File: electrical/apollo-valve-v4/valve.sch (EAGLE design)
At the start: 40 parts, among them J1 VALVE2, J2 VALVE1, J7 455-1750-1-ND, U1 DRV8806-SSOP, U2 DRV8806-SSOP, U3 TPS54202

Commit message: Add initial layout for the Valve board. Fully routed, with plenty of room to potentially add the steppers back
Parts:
- added C9: 100uF, SparkFun-Capacitors:100UF-POLAR-25V-20%(ELEC)
- added J3: (no value), SparkFun-Connectors:CONN_023.5MM
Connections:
- net +24V: now also C9.+, J3.1
- net GND: now also C9.-, J3.2
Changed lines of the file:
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@@
 <part name="J7" library="SparkFun-Connectors" deviceset="CONN_03" device="" value="455-1750-1-ND"/>
 <part name="R6" library="apollo-ctrl-v4" deviceset="RESISTOR" device="0805-RES" value="100K"/>
+<part name="J3" library="SparkFun-Connectors" deviceset="CONN_02" device="3.5MM"/>
+<part name="GND10" library="supply1" deviceset="GND" device=""/>
+<part name="P+6" library="supply1" deviceset="+24V" device=""/>
+<part name="C9" library="SparkFun-Capacitors" deviceset="100UF-POLAR" device="-25V-20%(ELEC)" value="100uF"/>
 </parts>
 <sheets>
@@
 <attribute name="NAME" x="140.97" y="87.4014" size="1.778" layer="95" rot="R180"/>
 <attribute name="VALUE" x="140.97" y="92.202" size="1.778" layer="96" rot="R180"/>
+</instance>
+<instance part="J3" gate="G$1" x="162.56" y="71.12" smashed="yes" rot="R180">
+<attribute name="VALUE" x="165.1" y="75.946" size="1.778" layer="96" font="vector" rot="R180"/>
+<attribute name="NAME" x="165.1" y="65.532" size="1.778" layer="95" font="vector" rot="R180"/>
+</instance>
+<instance part="GND10" gate="1" x="152.4" y="58.42" smashed="yes">
+<attribute name="VALUE" x="149.86" y="55.88" size="1.778" layer="96"/>
+</instance>
+<instance part="P+6" gate="1" x="152.4" y="76.2" smashed="yes">
+<attribute name="VALUE" x="149.86" y="71.12" size="1.778" layer="96" rot="R90"/>
+</instance>
+<instance part="C9" gate="G$1" x="142.24" y="68.58" smashed="yes">
+<attribute name="NAME" x="143.256" y="69.215" size="1.778" layer="95" font="vector"/>
+<attribute name="VALUE" x="143.256" y="64.389" size="1.778" layer="96" font="vector"/>
 </instance>
 </instances>
@@
 <junction x="104.14" y="119.38"/>
 </segment>
+<segment>
+<pinref part="GND10" gate="1" pin="GND"/>
+<wire x1="152.4" y1="60.96" x2="152.4" y2="63.5" width="0.1524" layer="91"/>
+<pinref part="J3" gate="G$1" pin="2"/>
+<wire x1="152.4" y1="63.5" x2="152.4" y2="68.58" width="0.1524" layer="91"/>
+<wire x1="152.4" y1="68.58" x2="154.94" y2="68.58" width="0.1524" layer="91"/>
+<pinref part="C9" gate="G$1" pin="-"/>
+<wire x1="142.24" y1="63.5" x2="152.4" y2="63.5" width="0.1524" layer="91"/>
+<junction x="152.4" y="63.5"/>
+</segment>
 </net>
 <net name="+24V" class="0">
@@
 <junction x="63.5" y="60.96"/>
 </segment>
+<segment>
+<pinref part="P+6" gate="1" pin="+24V"/>
+<wire x1="152.4" y1="73.66" x2="152.4" y2="71.12" width="0.1524" layer="91"/>
+<pinref part="J3" gate="G$1" pin="1"/>
+<wire x1="152.4" y1="71.12" x2="154.94" y2="71.12" width="0.1524" layer="91"/>
+<pinref part="C9" gate="G$1" pin="+"/>
+<wire x1="142.24" y1="71.12" x2="152.4" y2="71.12" width="0.1524" layer="91"/>
+<junction x="152.4" y="71.12"/>
+</segment>
 </net>

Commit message: Add stepper drivers to the valve board schematic. No guarantee that they fit, but if they do not another board can be made.
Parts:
- removed J7: 455-1750-1-ND, SparkFun-Connectors:CONN_03
- added C10, C11, C13, C14, C17, C18, C20, C21: 0.1u, apollo-ctrl-v4:CAP0805
- added C12, C19: 10u, apollo-ctrl-v4:CAP0805
- added C15, C16, C22, C23: 0.01u, apollo-ctrl-v4:CAP0805
- added J4: STEP, SparkFun-Connectors:CONN_083.5MM-8
- added R10, R14, R20, R21: 22, apollo-ctrl-v4:RESISTOR0805-RES
- added R11: 13.3K, apollo-ctrl-v4:RESISTOR0805-RES
- added R12, R13, R18, R19: 0.1, SparkFun-Resistors:0.1OHM-1210-1/2W-1%
- added R15, R16, R17, R8, R9: 100K, apollo-ctrl-v4:RESISTOR0805-RES
- added U4, U5: TMC2660, apollo-ctrl-v4:TMC2660
- R3: value 680K -> 499K
- R4: value 120K -> 82K
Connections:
- removed net LCS: J7.2, R6.1, U1.LATCH, U2.LATCH
- new net +12V: C12.1, C13.1, C14.1, C19.1, C20.1, C21.1, U4.VHS, U4.VS, U4.VSA, U4.VSB, U5.VHS, U5.VS, U5.VSA, U5.VSB
- new net +3V3: C11.1, C18.1, R15.2, R6.2, U$1.PIN1, U4.VCC_IO, U5.VCC_IO
- new net 5VOUT1: C10.1, U4.5VOUT
- new net 5VOUT2: C17.1, U5.5VOUT
- new net BRA1: R10.2, R12.2, U4.BRA
- new net BRA2: R18.2, R20.2, U5.BRA
- new net BRB1: R13.2, R14.2, U4.BRB
- new net BRB2: R19.2, R21.2, U5.BRB
- new net DIR1: R8.2, U4.DIR
- new net DIR2: R16.2, U5.DIR
- new net RESET: R11.1, U1.RESET, U2.RESET
- new net S1A: J4.4, U4.OA1@1, U4.OA1@3
- new net S1B: J4.3, U4.OA2@1, U4.OA2@3
- new net S1C: J4.2, U4.OB1@1, U4.OB1@3
- new net S1D: J4.1, U4.OB2@1, U4.OB2@3
- new net S2A: J4.8, U5.OA1@1, U5.OA1@3
- new net S2B: J4.7, U5.OA2@1, U5.OA2@3
- new net S2C: J4.6, U5.OB1@1, U5.OB1@3
- new net S2D: J4.5, U5.OB2@1, U5.OB2@3
- new net SRA1: C15.1, R10.1, U4.SRA
- new net SRA2: C22.1, R20.1, U5.SRA
- new net SRB1: C16.1, R14.1, U4.SRB
- new net SRB2: C23.1, R21.1, U5.SRB
- new net STEP1: R9.2, U4.STEP
- new net STEP2: R17.2, U5.STEP
- net !LOE!: now also U4.!EN, U5.!EN
- net CIDO: now also U4.SDO, U5.SDO
- net CODI: now also U4.SDI, U5.SDI
- net CS1: now also U1.LATCH, U2.LATCH; no longer J7.1, R6.2
- net CS2: now also R6.1, U4.!CS; no longer J7.3
- net CS3: now also R15.1, U5.!CS
- net GND: now also C10.2, C11.2, C12.2, C13.2, C14.2, C15.2, C16.2, C17.2, C18.2, C19.2, C20.2, C21.2, C22.2, C23.2, R11.2, R12.1, R13.1, R16.1, R17.1, R18.1, R19.1, R8.1, R9.1, U4.CLK, U4.GND@1, U4.GND@2, U4.GND@3, U4.TST_MODE, U5.CLK, U5.GND@1, U5.GND@2, U5.GND@3, U5.TST_MODE
- net SCK: now also U4.SCK, U5.SCK
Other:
- moved on the sheet: C1, C2, R6

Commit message: Remove the Trinamics bipolar stepper drivers and add unipolar stepper drivers instead (as the motors are cheaper and more available).
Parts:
- removed C18, C20, C21: 0.1u, apollo-ctrl-v4:CAP0805
- removed C19: 10u, apollo-ctrl-v4:CAP0805
- removed C22, C23: 0.01u, apollo-ctrl-v4:CAP0805
- removed R16, R17: 100K, apollo-ctrl-v4:RESISTOR0805-RES
- removed R18, R19: 0.1, SparkFun-Resistors:0.1OHM-1210-1/2W-1%
- removed R20, R21: 22, apollo-ctrl-v4:RESISTOR0805-RES
- added D10, D11, D12, D13, D14, D15, D16, D17, D18, D27, D28, D29, D30, D31, D32, D33: BAT46, SparkFun-DiscreteSemi:DIODE-SCHOTTKY-BAT60A
- added D9: SMBJ24A, diode:DIODE-SMB
- added J5: S2, SparkFun-Connectors:CONN_05JST
- added L2: VLS6045EX-220M, apollo-ctrl-v4:VLS6045EX-H
- added U6: TPS54202, apollo-ctrl-v4:TPS54202
- C12: value 10u -> 0.1u
- C13: value 0.1u -> 10u
- C15: value 0.01u -> 22u
- C16: value 0.01u -> 47u; device apollo-ctrl-v4:CAP0805 -> apollo-ctrl-v4:CAP_POLC
- C17: value 0.1u -> 100p
- D1, D19, D2, D20, D21, D22, D23, D24, D25, D26, D3, D4, D5, D6, D7, D8: value B340A -> BAT46; device SparkFun-DiscreteSemi:DIODE-SCHOTTKY-B340A -> SparkFun-DiscreteSemi:DIODE-SCHOTTKY-BAT60A
- J4: value STEP -> S1; device SparkFun-Connectors:CONN_083.5MM-8 -> SparkFun-Connectors:CONN_05JST
- L1: value VLS6045EX-H -> VLS6045EX-150M
- R10: value 22 -> 5.23K
- R11: value 13.3K -> 2.2K
- R12: value 0.1 -> 100K; device SparkFun-Resistors:0.1OHM-1210-1/2W-1% -> apollo-ctrl-v4:RESISTOR0805-RES
- R13: value 0.1 -> 499K; device SparkFun-Resistors:0.1OHM-1210-1/2W-1% -> apollo-ctrl-v4:RESISTOR0805-RES
- R14: value 22 -> 82K
- R15: value 100K -> 49.9
- R6, R7, R8: value 100K -> 2.2K
- R9: value 100K -> EMPTY
- U4, U5: value TMC2660 -> DRV8806-SSOP; device apollo-ctrl-v4:TMC2660 -> apollo-ctrl-v4:DRV8806-SSOP
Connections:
- net VEN renamed VEN1
- removed net 5VOUT1: C10.1, U4.5VOUT
- removed net 5VOUT2: C17.1, U5.5VOUT
- removed net BRA1: R10.2, R12.2, U4.BRA
- removed net BRA2: R18.2, R20.2, U5.BRA
- removed net BRB1: R13.2, R14.2, U4.BRB
- removed net BRB2: R19.2, R21.2, U5.BRB
- removed net DIR1: R8.2, U4.DIR
- removed net DIR2: R16.2, U5.DIR
- removed net SRA1: C15.1, R10.1, U4.SRA
- removed net SRA2: C22.1, R20.1, U5.SRA
- removed net SRB1: C16.1, R14.1, U4.SRB
- removed net SRB2: C23.1, R21.1, U5.SRB
- removed net STEP1: R9.2, U4.STEP
- removed net STEP2: R17.2, U5.STEP
- new net BOOT2: C14.1, U6.BOOT
- new net CIDO2: R6.1, R9.2, U2.SDATOUT, U4.SDATIN
- new net CIDO3: R8.1, U4.SDATOUT, U5.SDATIN
- new net FB2: C17.2, R10.1, R12.2, U6.FB
- new net FF2: C17.1, R12.1, R15.2
- new net SW2: C14.2, L2.1, U6.SW
- new net VEN2: R13.1, R14.2, U6.EN
- net !FAULT!: now also U4.!NFAULT, U5.!NFAULT
- net !LOE!: now also U4.!NENBL, U5.!NENBL; no longer U4.!EN, U5.!EN
- net +12V: now also C10.1, C11.1, C15.1, C16.+, D14.C, D15.C, D16.C, D17.C, D30.C, D31.C, D32.C, D33.C, L2.2, R15.1, U4.VCLAMP, U4.VM, U5.VCLAMP, U5.VM; no longer C12.1, C13.1, C14.1, C19.1, C20.1, C21.1, U4.VHS, U4.VS, U4.VSA, U4.VSB, U5.VHS, U5.VS, U5.VSA, U5.VSB
- net +24V: now also C12.1, C13.1, D9.C, R13.2, U6.VIN
- net +3V3: no longer C11.1, C18.1, R15.2, R6.2, U4.VCC_IO, U5.VCC_IO
- net +5V: now also R6.2, R8.2
- net CIDO: now also R9.1, U5.SDATOUT; no longer U2.SDATOUT, U4.SDO, U5.SDO
- net CODI: no longer U4.SDI, U5.SDI
- net CS1: now also U4.LATCH, U5.LATCH
- net CS2: no longer R6.1, U4.!CS
- net CS3: no longer R15.1, U5.!CS
- net GND: now also C16.-, D10.A, D11.A, D12.A, D13.A, D18.A, D27.A, D28.A, D29.A, D9.A, J4.3, J5.3, R10.2, R14.1, U4.EP, U4.GND1, U4.GND2, U5.EP, U5.GND1, U5.GND2, U6.GND; no longer C14.2, C16.2, C17.2, C18.2, C19.2, C20.2, C21.2, C22.2, C23.2, R12.1, R13.1, R16.1, R17.1, R18.1, R19.1, R8.1, R9.1, U4.CLK, U4.GND@1, U4.GND@2, U4.GND@3, U4.TST_MODE, U5.CLK, U5.GND@1, U5.GND@2, U5.GND@3, U5.TST_MODE
- net RESET: now also U4.RESET, U5.RESET
- net S1A: now also D13.C, D17.A, J4.5, U4.OUT1; no longer J4.4, U4.OA1@1, U4.OA1@3
- net S1B: now also D12.C, D16.A, J4.4, U4.OUT2; no longer J4.3, U4.OA2@1, U4.OA2@3
- net S1C: now also D11.C, D15.A, U4.OUT3; no longer U4.OB1@1, U4.OB1@3
- net S1D: now also D10.C, D14.A, U4.OUT4; no longer U4.OB2@1, U4.OB2@3
- net S2A: now also D29.C, D33.A, J5.5, U5.OUT1; no longer J4.8, U5.OA1@1, U5.OA1@3
- net S2B: now also D28.C, D32.A, J5.4, U5.OUT2; no longer J4.7, U5.OA2@1, U5.OA2@3
- net S2C: now also D27.C, D31.A, J5.2, U5.OUT3; no longer J4.6, U5.OB1@1, U5.OB1@3
- net S2D: now also D18.C, D30.A, J5.1, U5.OUT4; no longer J4.5, U5.OB2@1, U5.OB2@3
- net SCK: now also U4.SCLK, U5.SCLK; no longer U4.SCK, U5.SCK
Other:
- moved on the sheet: C10, C11, C12, C13, C14, C15, C17, R10, R12, R13, R14, R15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

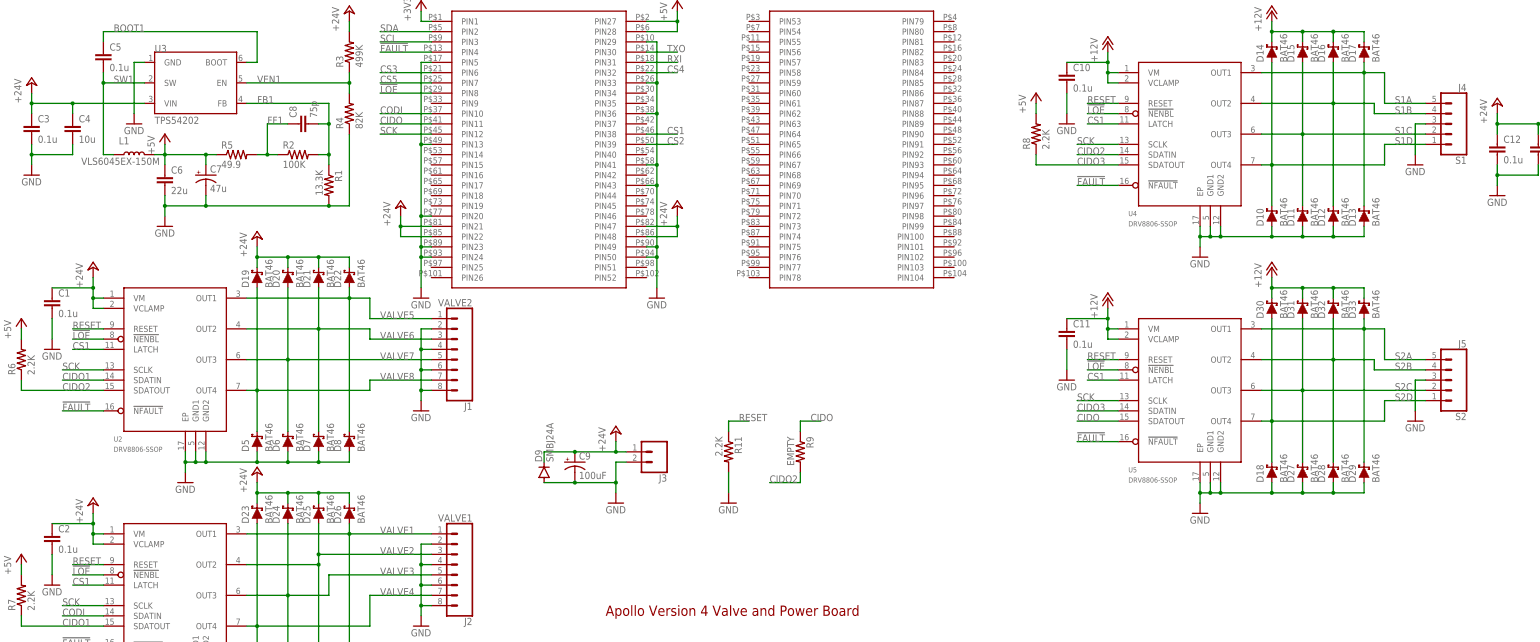
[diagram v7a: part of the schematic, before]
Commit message: First layout pass for complete valve board
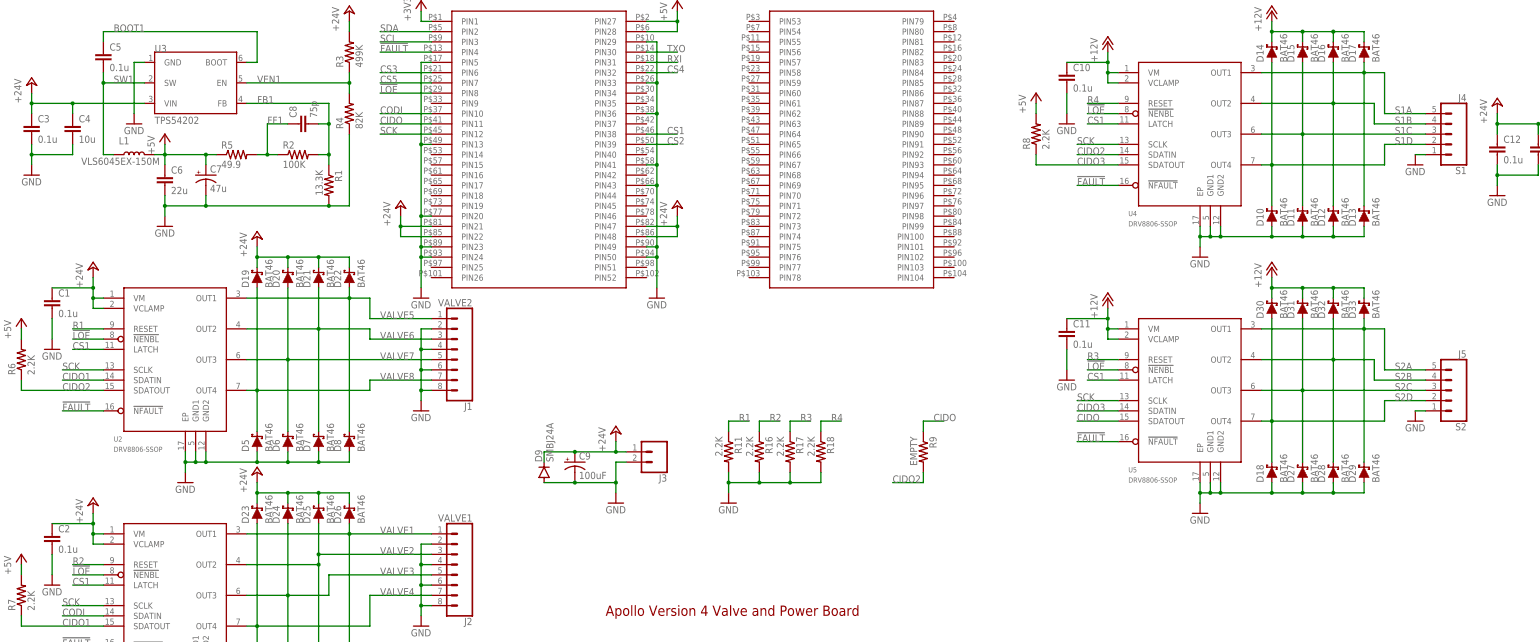
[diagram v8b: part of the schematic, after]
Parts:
- added R16, R17, R18: 2.2K, apollo-ctrl-v4:RESISTOR0805-RES
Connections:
- removed net RESET: R11.1, U1.RESET, U2.RESET, U4.RESET, U5.RESET
- new net R1: R11.1, U2.RESET
- new net R2: R16.1, U1.RESET
- new net R3: R17.1, U5.RESET
- new net R4: R18.1, U4.RESET
- net GND: now also J4.1, J5.1, R16.2, R17.2, R18.2; no longer J4.3, J5.3
- net S1C: now also J4.3; no longer J4.2
- net S1D: now also J4.2; no longer J4.1
- net S2C: now also J5.3; no longer J5.2
- net S2D: now also J5.2; no longer J5.1
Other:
- moved on the sheet: J4, J5, R9
